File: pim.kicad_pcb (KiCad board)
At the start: 2 copper layers, 100 x 65.3 mm, 13 parts, among them J1 DE9_Plug, J2 DE9_Plug, J3 Conn_01x20_Pin, J4 Conn_01x03_MountingPin, U1 RaspberryPi_Pico_W

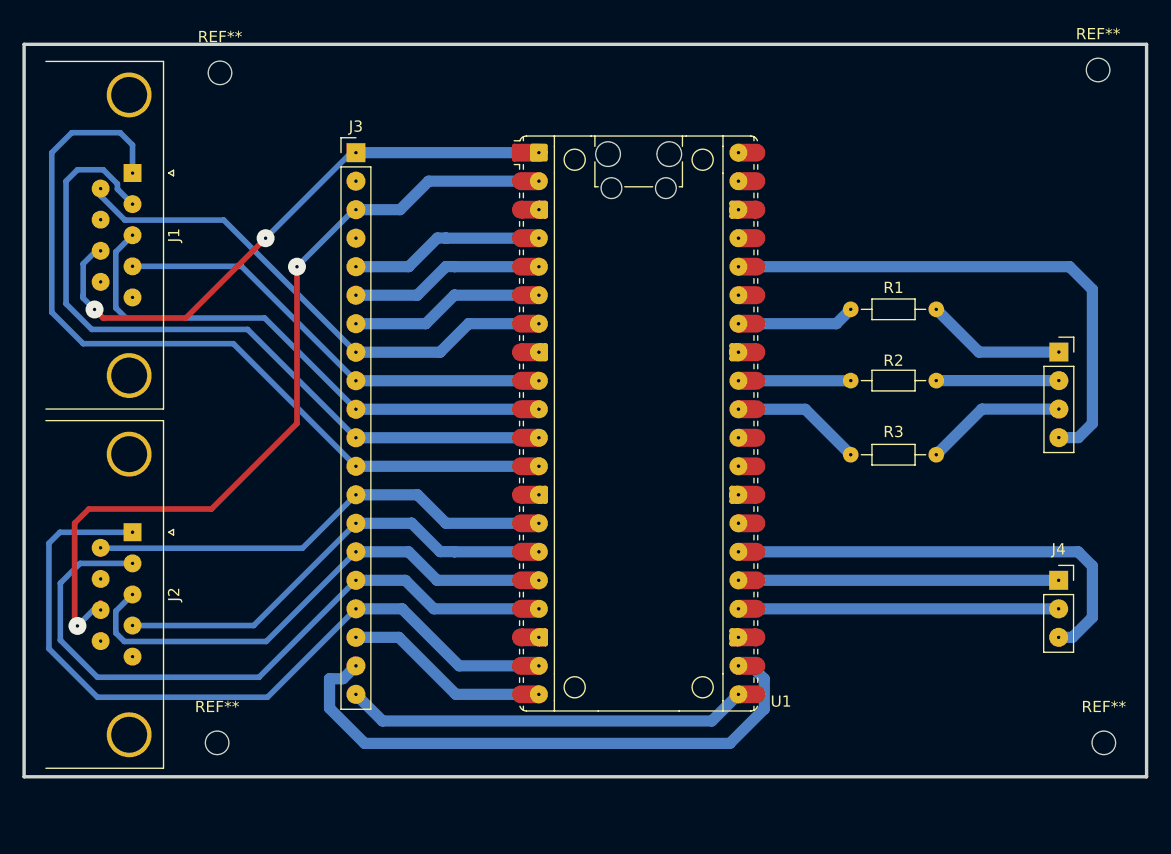
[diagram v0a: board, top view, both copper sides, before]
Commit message: several improvements PCB size, vias, footprints sizes restoring
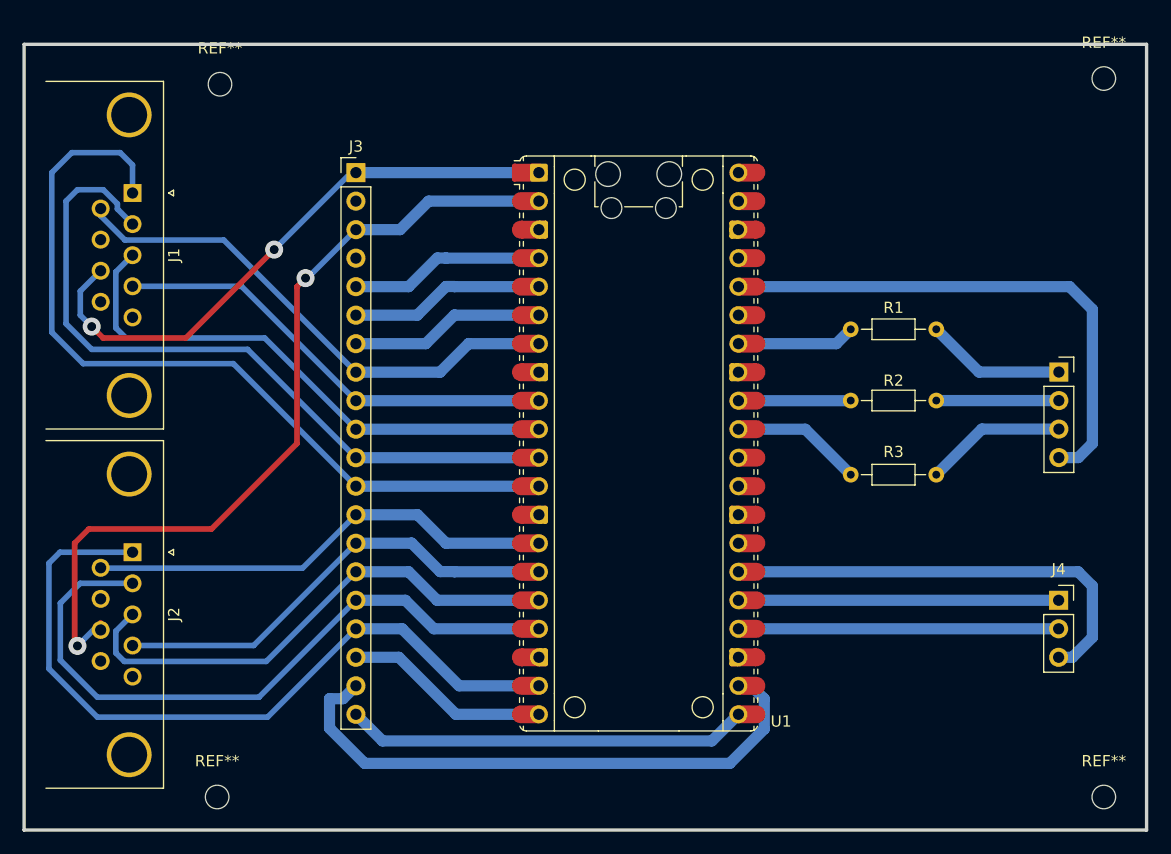
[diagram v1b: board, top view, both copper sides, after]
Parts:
- moved REF** 4.83 mm to (116.1, 81.0)
- moved REF** 4.83 mm to (37.1, 81.0)
- moved J1 1.78 mm to (29.5, 27.2)
- moved D1 1.78 mm to (112.1, 43.2)
- moved J2 1.78 mm to (29.5, 59.2)
- moved J3 1.78 mm to (49.4, 25.4)
- moved J4 1.78 mm to (112.1, 63.5)
- moved R1 1.78 mm to (93.5, 39.4)
- moved R2 1.78 mm to (93.5, 45.7)
- moved R3 1.78 mm to (93.5, 52.3)
- moved U1 1.78 mm to (74.6, 49.5)
- moved REF** 1.02 mm to (37.3, 17.5)
- moved REF** 0.92 mm to (116.1, 17.0)
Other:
- board size 100 x 65.3 mm -> 100 x 70 mm

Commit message: adding version print
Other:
- board text added: "v0.0.2"
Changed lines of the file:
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@@
 		(fp_arc
 			(start 10.579676 25.189937)
-			(mid 10.357949 25.493953)
+			(mid 10.357946 25.493957)
 			(end 10 25.61)
 			(stroke
@@
 		(layer "B.Fab")
 		(effects
+			(font
+				(size 1.5 1.5)
+				(thickness 0.3)
+				(bold yes)
+			)
+			(justify right bottom mirror)
+		)
+	)
+	(gr_text "v0.0.2"
+		(at 95.504 81.788 0)
+		(layer "B.Fab")
+		(effects

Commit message: some adjustments
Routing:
- net /M-8: track 74.9 -> 72.2 mm
- net /M-b: track 51.1 -> 50.4 mm
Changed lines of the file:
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@@
 	)
 	(gr_text "PIMMO-PORTS-64"
-		(at 87.376 79.248 0)
+		(at 109.474 78.74 0)
 		(layer "B.Fab")
 		(effects
@@
 				(bold yes)
 			)
-			(justify right bottom mirror)
+			(justify right bottom)
 		)
 	)
 	(gr_text "v0.0.2"
-		(at 95.504 81.788 0)
+		(at 95.758 81.28 0)
 		(layer "B.Fab")
 		(effects
@@
 	)
 	(segment
-		(start 85.827428 74.961)
-		(end 85.827428 72.28863)
+		(start 50.228428 78.03)
+		(end 47.244 75.045572)
 		(width 1)
 		(layer "B.Cu")
@@
 	)
 	(segment
+		(start 83.527428 71.12)
+		(end 85.598 73.190572)
+		(width 1)
+		(layer "B.Cu")
+		(net 12)
+	)
+	(segment
+		(start 85.598 73.190572)
+		(end 85.598 75.190428)
+		(width 1)
+		(layer "B.Cu")
+		(net 12)
+	)
+	(segment
+		(start 47.244 75.045572)
+		(end 47.244 72.898)
+		(width 1)
+		(layer "B.Cu")
+		(net 12)
+	)
+	(segment
+		(start 85.598 75.190428)
+		(end 82.758428 78.03)
+		(width 1)
+		(layer "B.Cu")
+		(net 12)
+	)
+	(segment
 		(start 82.758428 78.03)
-		(end 85.827428 74.961)
+		(end 50.228428 78.03)
 		(width 1)
 		(layer "B.Cu")
@@
 	)
 	(segment
-		(start 50.228428 78.03)
-		(end 82.758428 78.03)
-		(width 1)
-		(layer "B.Cu")
-		(net 12)
-	)
-	(segment
-		(start 48.299509 72.267919)
-		(end 47.097428 72.267919)
-		(width 1)
-		(layer "B.Cu")
-		(net 12)
-	)
-	(segment
-		(start 49.447428 71.12)
-		(end 48.299509 72.267919)
-		(width 1)
-		(layer "B.Cu")
-		(net 12)
-	)
-	(segment
-		(start 85.827428 72.28863)
-		(end 84.658798 71.12)
-		(width 1)
-		(layer "B.Cu")
-		(net 12)
-	)
-	(segment
-		(start 47.097428 72.267919)
-		(end 47.097428 74.899)
-		(width 1)
-		(layer "B.Cu")
-		(net 12)
-	)
-	(segment
-		(start 47.097428 74.899)
-		(end 50.228428 78.03)
+		(start 47.244 72.898)
+		(end 49.022 71.12)
 		(width 1)
 		(layer "B.Cu")
@@
 	)
 	(segment
+		(start 36.576 57.15)
+		(end 44.196 49.53)
+		(width 0.5)
+		(layer "F.Cu")
+		(net 22)
+	)
+	(segment
+		(start 24.638 65.024)
+		(end 24.384 64.77)
+		(width 0.5)
+		(layer "F.Cu")
+		(net 22)
+	)
+	(segment
+		(start 24.384 58.42)
+		(end 25.654 57.15)
+		(width 0.5)
+		(layer "F.Cu")
+		(net 22)
+	)
+	(segment
+		(start 24.384 64.77)
+		(end 24.384 58.42)
+		(width 0.5)
+		(layer "F.Cu")
+		(net 22)
+	)
+	(segment
+		(start 44.196 49.53)
+		(end 44.196 35.56)
+		(width 0.5)
+		(layer "F.Cu")
+		(net 22)
+	)
+	(segment
+		(start 44.196 35.56)
+		(end 44.958 34.798)
+		(width 0.5)
+		(layer "F.Cu")
+		(net 22)
+	)
+	(segment
 		(start 25.654 57.15)
-		(end 24.384 58.42)
-		(width 0.5)
-		(layer "F.Cu")
-		(net 22)
-	)
-	(segment
-		(start 24.384 67.31)
-		(end 24.638 67.564)
-		(width 0.5)
-		(layer "F.Cu")
-		(net 22)
-	)
-	(segment
-		(start 44.196 35.56)
-		(end 44.196 49.53)
-		(width 0.5)
-		(layer "F.Cu")
-		(net 22)
-	)
-	(segment
-		(start 44.958 34.798)
-		(end 44.196 35.56)
-		(width 0.5)
-		(layer "F.Cu")
-		(net 22)
-	)
-	(segment
-		(start 44.196 49.53)
 		(end 36.576 57.15)
-		(width 0.5)
-		(layer "F.Cu")
-		(net 22)
-	)
-	(segment
-		(start 36.576 57.15)
-		(end 25.654 57.15)
-		(width 0.5)
-		(layer "F.Cu")
-		(net 22)
-	)
-	(segment
-		(start 24.384 58.42)
-		(end 24.384 67.31)
 		(width 0.5)
 		(layer "F.Cu")
@@
 	)
 	(via
-		(at 24.638 67.564)
+		(at 24.638 65.024)
 		(size 1.6)
 		(drill 0.8)
@@
 	)
 	(segment
+		(start 24.638 65.024)
+		(end 25.759 66.145)
+		(width 0.5)
+		(layer "B.Cu")
+		(net 22)
+	)
+	(segment
 		(start 53.386428 30.48)
 		(end 55.926428 27.94)
@@
 	)
 	(segment
-		(start 26.057 66.145)
-		(end 26.706331 66.145)
-		(width 0.5)
-		(layer "B.Cu")
-		(net 22)
-	)
-	(segment
-		(start 24.638 67.564)
-		(end 26.057 66.145)
-		(width 0.5)
-		(layer "B.Cu")
-		(net 22)
-	)
-	(segment
 		(start 55.926428 27.94)
 		(end 65.747428 27.94)
@@
 	)
 	(segment
+		(start 25.759 66.145)
+		(end 26.706331 66.145)
+		(width 0.5)
+		(layer "B.Cu")
+		(net 22)
+	)
+	(segment
 		(start 49.447428 30.48)
 		(end 45.129428 34.798)
@@
 	)
 	(zone
-		(net 22)
-		(net_name "/M-8")
+		(net 13)
+		(net_name "/M-i")
 		(layer "F.Cu")
 		(name "$teardrop_padvia$")
 		(hatch full 0.1)
-		(priority 30000)
+		(priority 30002)
 		(attr
 			(teardrop
@@
 		(polygon
 			(pts
-				(xy 43.946 36.082369) (xy 44.446 36.082369) (xy 45.264147 35.537104) (xy 44.958 34.797) (xy 44.158 34.798)
+				(xy 27.087159 40.382) (xy 27.087159 39.882) (xy 26.647104 38.809853) (xy 25.907 39.116) (xy 25.601853 39.855104)
 			)
 		)
@@
 		(name "$teardrop_padvia$")
 		(hatch full 0.1)
-		(priority 30000)
+		(priority 30001)
 		(attr
 			(teardrop
@@
 	)
 	(zone
-		(net 13)
-		(net_name "/M-i")
+		(net 22)
+		(net_name "/M-8")
 		(layer "F.Cu")
 		(name "$teardrop_padvia$")
 		(hatch full 0.1)
-		(priority 30000)
+		(priority 30003)
 		(attr
 			(teardrop
@@
 		(polygon
 			(pts
-				(xy 27.087159 40.382) (xy 27.087159 39.882) (xy 26.647104 38.809853) (xy 25.907 39.116) (xy 25.601853 39.855104)
+				(xy 43.946 36.082369) (xy 44.446 36.082369) (xy 45.264147 35.537104) (xy 44.958 34.797) (xy 44.158 34.798)
 			)
 		)
@@
 		(polygon
 			(pts
-				(xy 24.634 66.014523) (xy 24.134 66.014523) (xy 23.838 67.564) (xy 24.638 67.565) (xy 25.377104 67.257853)
+				(xy 24.634 63.474523) (xy 24.134 63.474523) (xy 23.838 65.024) (xy 24.638 65.025) (xy 25.377104 64.717853)
 			)
 		)
 	)
 	(zone
-		(net 22)
-		(net_name "/M-8")
+		(net 13)
+		(net_name "/M-i")
 		(layer "B.Cu")
 		(name "$teardrop_padvia$")
 		(hatch full 0.1)
-		(priority 30000)
+		(priority 30003)
 		(attr
 			(teardrop
@@
 		(polygon
 			(pts
-				(xy 46.334812 33.94617) (xy 45.981258 33.592616) (xy 44.651853 34.058896) (xy 44.957293 34.798707)
-				(xy 45.697104 35.104147)
+				(xy 25.142 37.936841) (xy 24.642 37.936841) (xy 25.168896 39.422147) (xy 25.908 39.117) (xy 26.214147 38.376896)
 			)
 		)
 	)
 	(zone
-		(net 13)
-		(net_name "/M-i")
+		(net 22)
+		(net_name "/M-8")
 		(layer "B.Cu")
 		(name "$teardrop_padvia$")
 		(hatch full 0.1)
-		(priority 30000)
+		(priority 30001)
 		(attr
 			(teardrop
@@
 		(polygon
 			(pts
-				(xy 25.142 37.936841) (xy 24.642 37.936841) (xy 25.168896 39.422147) (xy 25.908 39.117) (xy 26.214147 38.376896)
+				(xy 46.334812 33.94617) (xy 45.981258 33.592616) (xy 44.651853 34.058896) (xy 44.957293 34.798707)
+				(xy 45.697104 35.104147)
 			)
 		)
 	)
 	(zone
-		(net 13)
-		(net_name "/M-i")
+		(net 22)
+		(net_name "/M-8")
 		(layer "B.Cu")
 		(name "$teardrop_padvia$")
 		(hatch full 0.1)
-		(priority 30000)
+		(priority 30002)
 		(attr
 			(teardrop
@@
 		(polygon
 			(pts
-				(xy 43.472147 31.303407) (xy 43.118593 30.949853) (xy 41.857853 31.518896) (xy 42.163293 32.258707)
-				(xy 42.903104 32.564147)
+				(xy 25.773666 66.395) (xy 25.773666 65.895) (xy 25.377104 64.717853) (xy 24.637 65.024) (xy 24.331853 65.763104)
 			)
 		)
 	)
 	(zone
-		(net 22)
-		(net_name "/M-8")
+		(net 13)
+		(net_name "/M-i")
 		(layer "B.Cu")
 		(name "$teardrop_padvia$")
@@
 		(polygon
 			(pts
-				(xy 25.946147 66.609407) (xy 25.592593 66.255853) (xy 24.331853 66.824896) (xy 24.637293 67.564707)
-				(xy 25.377104 67.870147)
-			)
-		)
+				(xy 43.472147 31.303407) (xy 43.118593 30.949853) (xy 41.857853 31.518896) (xy 42.163293 32.258707)
+				(xy 42.903104 32.564147)
+			)
+		)

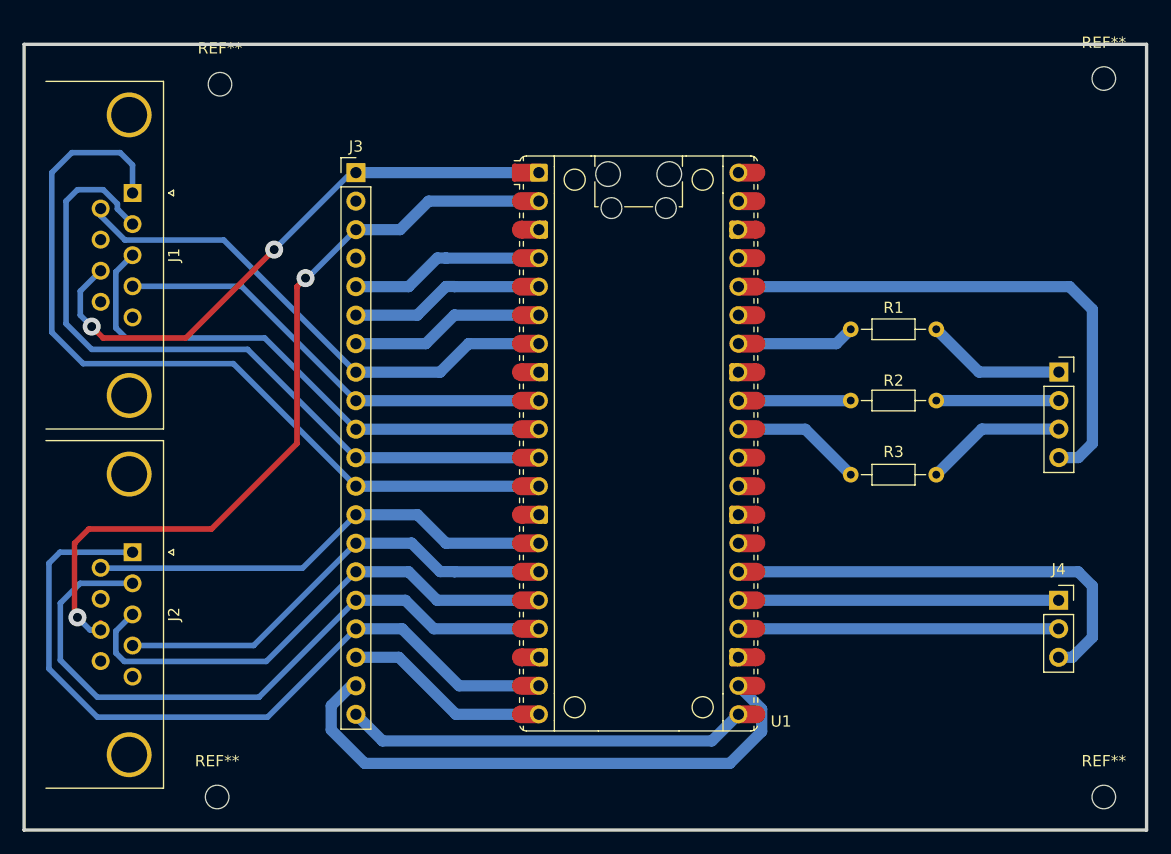
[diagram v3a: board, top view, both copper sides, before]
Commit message: Invert pico
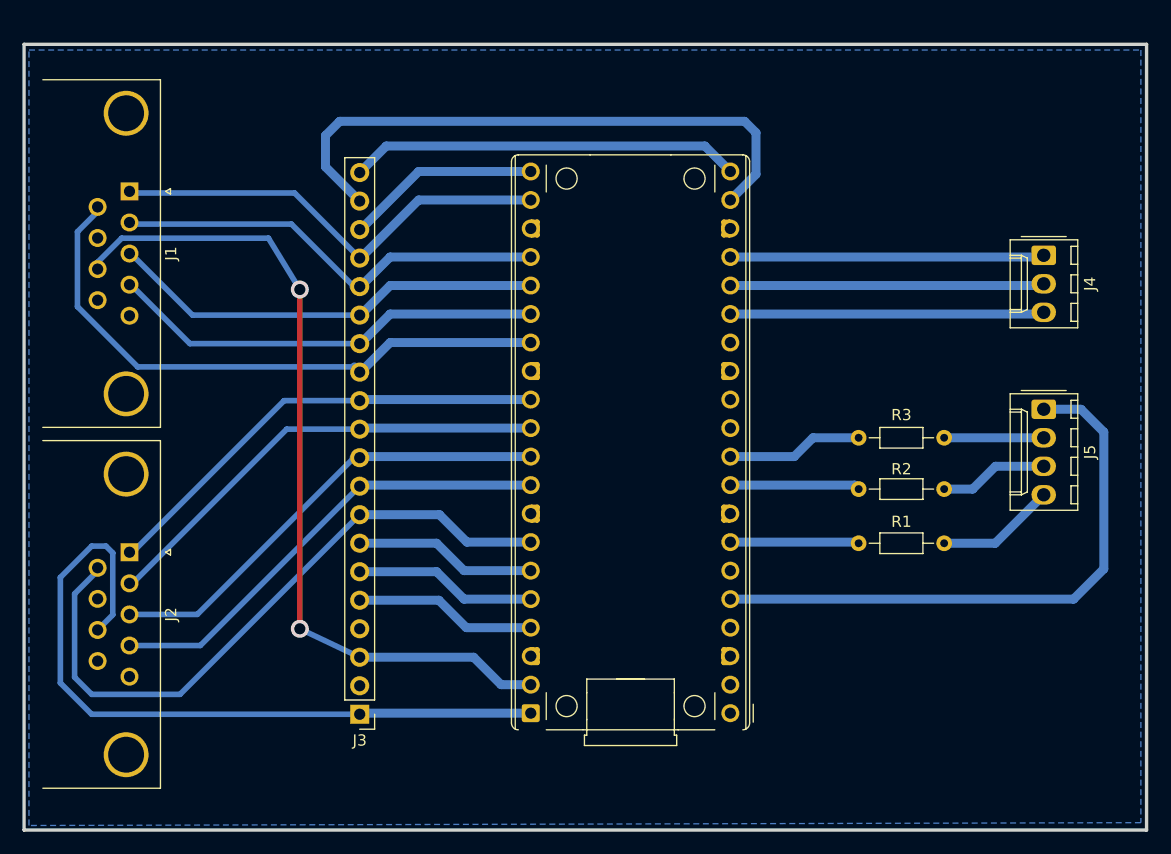
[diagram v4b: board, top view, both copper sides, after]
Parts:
- removed D1: LED_RGBA, Connector_PinSocket_2.54mm:PinSocket_1x04_P2.54mm_Vertical
- removed REF** (x4): MountingHole_2.1mm, MountingHole:MountingHole_2.1mm
- added J5: RGB Led, Connector_Molex:Molex_KK-254_AE-6410-04A_1x04_P2.54mm_Vertical, F.Cu at (110.7, 46.5)
- J1: value DE9_Plug -> Joystick1
- J2: value DE9_Plug -> Joystick2
- J4: value Conn_01x03_MountingPin -> Rasp PI Interface; footprint Connector_PinSocket_2.54mm:PinSocket_1x03_P2.54mm_Vertical -> Connector_Molex:Molex_KK-254_AE-6410-03A_1x03_P2.54mm_Vertical
- R1: value 5 -> 5k
- U1: footprint Module_RaspberryPi_Pico:RaspberryPi_Pico_Common -> Module_RaspberryPi_Pico:RaspberryPi_Pico_Common_THT
- moved J3 48.3 mm to (49.8, 73.7), turned to 180 degrees
- moved J4 30.8 mm to (110.7, 32.8), turned to -90 degrees
- moved R1 19.1 mm to (94.2, 58.4)
- moved R2 7.92 mm to (94.2, 53.6)
- moved R3 3.36 mm to (94.2, 49.0)
- moved U1 0.73 mm to (73.9, 49.4), turned to 180 degrees
- moved J1 0.31 mm to (29.3, 27.1)
- moved J2 0.27 mm to (29.3, 59.2)
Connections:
- J1 pad 1: /M-0 -> /M-d
- J1 pad 2: /M-1 -> /M-e
- J1 pad 3: /M-2 -> /M-f
- J1 pad 4: /M-3 -> /M-g
- J1 pad 6: /M-4 -> /M-h
- J1 pad 8: /M-i -> /M-8
- J2 pad 1: /M-d -> /M-0
- J2 pad 2: /M-e -> /M-1
- J2 pad 3: /M-f -> /M-2
- J2 pad 4: /M-g -> /M-3
- J2 pad 6: /M-h -> /M-4
- J2 pad 8: /M-8 -> /M-i
- J4 pad 1: /PI-09 -> /PI-10
- J4 pad 2: /PI-10 -> /PI-09
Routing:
- net /M-0: track 74.2 -> 41.1 mm
- net /M-d: track 68.1 -> 40.0 mm
- net /M-1: track 66.3 -> 41.2 mm
- net /M-e: track 60.9 -> 38.9 mm
- net /M-4: track 46.5 -> 59.6 mm
- net /M-i: track 53.0 -> 66.0 mm, vias 2 -> 0
- net /PI-11: track 40.4 -> 28.0 mm
- net /M-h: track 42.1 -> 53.5 mm
- net /M-f: track 46.4 -> 38.8 mm
- net /M-2: track 48.5 -> 41.3 mm
- net Net-(J5-Pin_1): track 47.8 -> 52.8 mm
- net Net-(J5-Pin_2): track 12.6 -> 8.87 mm
- net /M-b: track 50.4 -> 53.3 mm
- net /M-8: track 72.2 -> 74.7 mm
- net /M-g: track 41.0 -> 38.7 mm
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- added copper zone on B.Cu, net GNDPWR
